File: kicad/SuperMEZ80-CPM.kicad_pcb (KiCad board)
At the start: 2 copper layers, 61 x 57.1 mm, 36 parts, among them J1 EMUZ80_0, J2 EMUZ80, J3 Conn_02x03_Odd_Even, J4 Conn_02x01, J5 Conn_02x02_Odd_Even, J6 SD Card slot, J7 SD Card slot, U1 Z80CPU, U2 AS6C4008

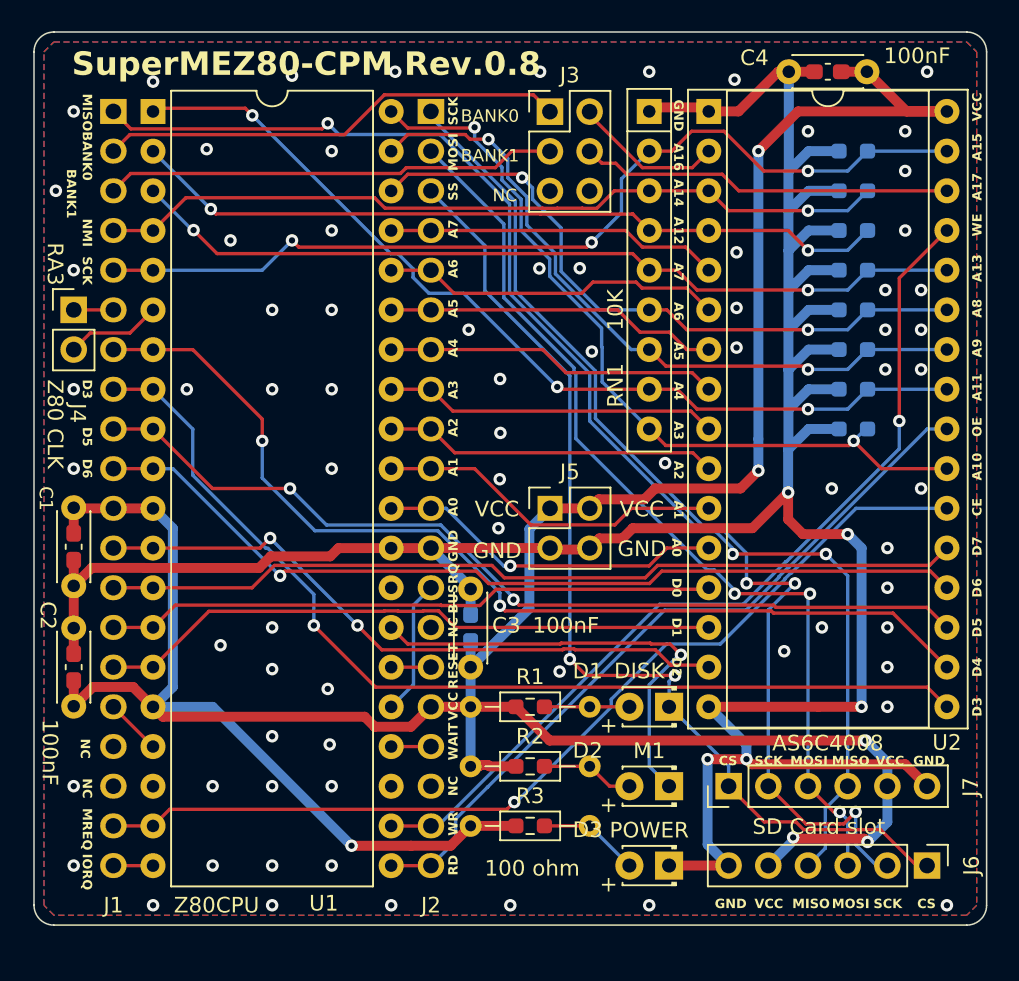
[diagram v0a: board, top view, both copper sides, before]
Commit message: Add SuperMEZ80-CPM version 1.0
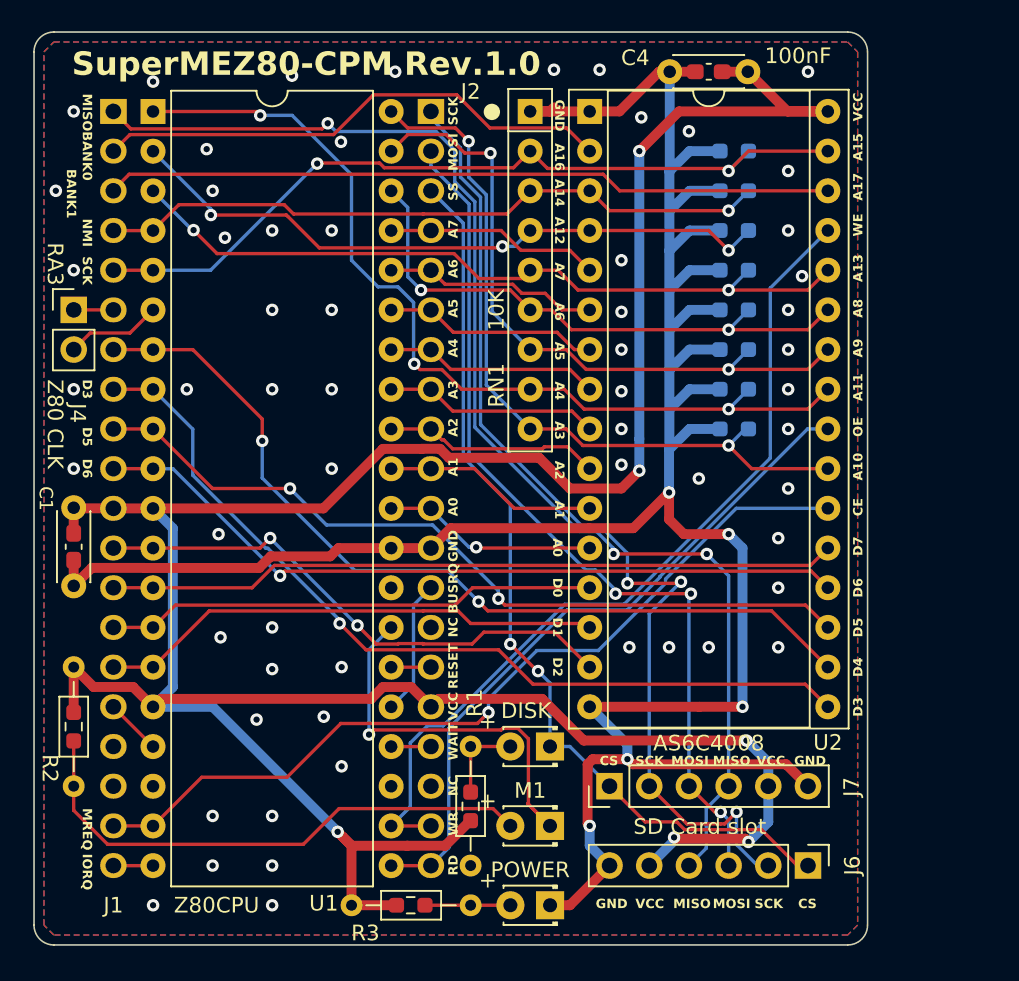
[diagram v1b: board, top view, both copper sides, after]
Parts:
- removed C2, C3: 100nF, Capacitor_THT:C_Disc_D4.3mm_W1.9mm_P5.00mm
- removed C6, C7: 100nF, Capacitor_SMD:C_0603_1608Metric_Pad1.08x0.95mm_HandSolder
- removed J3: Conn_02x03_Odd_Even, Connector_PinHeader_2.54mm:PinHeader_2x03_P2.54mm_Vertical
- removed J5: Conn_02x02_Odd_Even, Connector_PinHeader_2.54mm:PinHeader_2x02_P2.54mm_Vertical
- moved R5 29.3 mm to (78.7, 101.6), turned to -90 degrees
- moved R2 26.2 mm to (78.7, 97.8), turned to -90 degrees
- moved R1 10.2 mm to (104.1, 110.5), turned to 90 degrees
- moved R6 9.18 mm to (100.3, 113.0)
- moved R3 9.16 mm to (96.5, 113.0)
- moved D1 8.03 mm to (109.2, 102.9)
- moved D2 8.03 mm to (109.2, 108.0)
- moved D3 8.03 mm to (109.2, 113.0)
- moved C4 7.62 mm to (121.9, 59.7)
- moved C8 7.62 mm to (119.4, 59.7)
- moved J7 7.62 mm to (113.0, 105.4)
- moved R10 7.62 mm to (121.0, 72.4)
- moved R11 7.62 mm to (121.0, 74.9)
- moved R12 7.62 mm to (121.0, 77.5)
- moved R13 7.62 mm to (121.0, 80.0)
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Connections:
- J1 pad 2: BANK0 -> A16
- J1 pad 3: BANK1 -> A17
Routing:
- net BANK0: track 29.9 -> 0.00 mm
- net BANK1: track 29.0 -> 0.00 mm
- net Net-(D2-A): track 5.96 -> 34.7 mm
- net A16: track 9.67 -> 33.5 mm
- net A17: track 23.9 -> 46.6 mm
- net GND: track 185.9 -> 171.3 mm, vias 79 -> 65
- net D3: track 64.7 -> 56.0 mm
- net A0: track 22.3 -> 13.8 mm
- net A1: track 22.3 -> 13.8 mm
- net D7: track 55.1 -> 46.8 mm
- net D6: track 57.4 -> 49.1 mm
- net A15: track 60.2 -> 52.0 mm, vias 3 -> 2
- net A6: track 22.0 -> 13.8 mm
- net D4: track 64.5 -> 56.3 mm
- net D1: track 40.1 -> 32.1 mm
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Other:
- board size 61 x 57.1 mm -> 53.3 x 58.4 mm
- board text added: "Aug 17, 2023 @hanyazou"
- board text added: "SuperMEZ80-CPM Rev.1.0"
- board text added: "●"
- board text removed: "100 ohm"
- board text removed: "Jul 8, 2023 @hanyazou"
- board text removed: "SuperMEZ80-CPM Rev.0.8"

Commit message: Add SuperMEZ80-CPM version 1.1 and update README.md
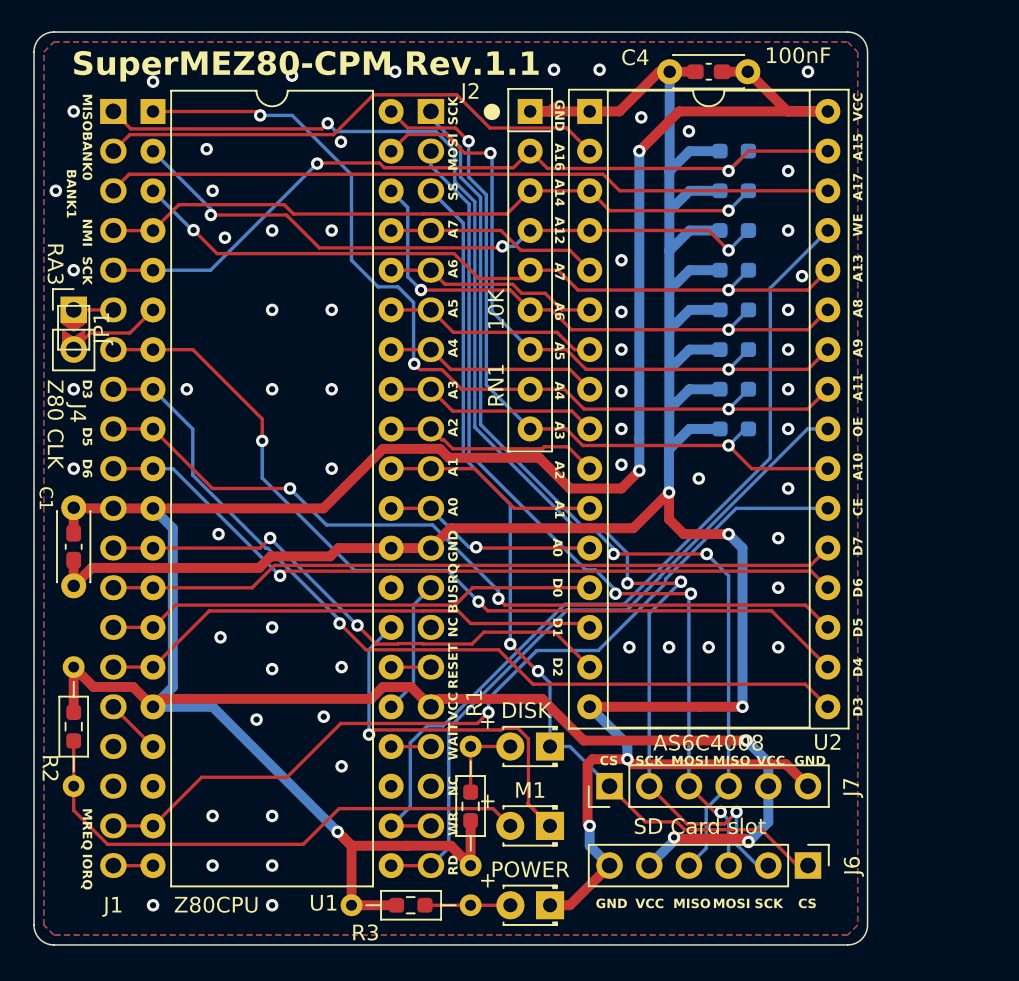
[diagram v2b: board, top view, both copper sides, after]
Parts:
- added JP1: Jumper_2_Open, Jumper:SolderJumper-2_P1.3mm_Open_TrianglePad1.0x1.5mm, F.Cu at (78.7, 76.1)
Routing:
- net VCC: track 192.6 -> 195.3 mm
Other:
- board text added: "Aug 25, 2023 @hanyazou"
- board text added: "SuperMEZ80-CPM Rev.1.1"
- board text removed: "Aug 17, 2023 @hanyazou"
- board text removed: "SuperMEZ80-CPM Rev.1.0"
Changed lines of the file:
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@@
       (drillshape 0)
       (scaleselection 1)
-      (outputdirectory "SuperMEZ80-CPM-1.0")
+      (outputdirectory "SuperMEZ80-CPM-1.1")
     )
   )
@@
     )
   )
+  (footprint "Jumper:SolderJumper-2_P1.3mm_Open_TrianglePad1.0x1.5mm" (layer "F.Cu")
+    (at 78.74 76.073 -90)
+    (descr "SMD Solder Jumper, 1x1.5mm Triangular Pads, 0.3mm gap, open")
+    (tags "solder jumper open")
+    (property "Sheetfile" "SuperMEZ80-CPM.kicad_sch")
+    (property "Sheetname" "")
+    (property "ki_description" "Jumper, 2-pole, open")
+    (property "ki_keywords" "Jumper SPST")
+    (attr exclude_from_pos_files)
+    (fp_text reference "JP1" (at 0 -1.8 90) (layer "F.SilkS")
+        (effects (font (size 1 1) (thickness 0.15)))
+    )
+    (fp_text value "Jumper_2_Open" (at 0 1.9 90) (layer "F.Fab")
+        (effects (font (size 1 1) (thickness 0.15)))
+    )
+    (fp_line (start -1.4 -1) (end 1.4 -1)
+      (stroke (width 0.12) (type solid)) (layer "F.SilkS"))
+    (fp_line (start -1.4 1) (end -1.4 -1)
+      (stroke (width 0.12) (type solid)) (layer "F.SilkS"))
+    (fp_line (start 1.4 -1) (end 1.4 1)
+      (stroke (width 0.12) (type solid)) (layer "F.SilkS"))
+    (fp_line (start 1.4 1) (end -1.4 1)
+      (stroke (width 0.12) (type solid)) (layer "F.SilkS"))
+    (fp_line (start -1.65 -1.25) (end -1.65 1.25)
+      (stroke (width 0.05) (type solid)) (layer "F.CrtYd"))
+    (fp_line (start -1.65 -1.25) (end 1.65 -1.25)
+      (stroke (width 0.05) (type solid)) (layer "F.CrtYd"))
+    (fp_line (start 1.65 1.25) (end -1.65 1.25)
+      (stroke (width 0.05) (type solid)) (layer "F.CrtYd"))
+    (fp_line (start 1.65 1.25) (end 1.65 -1.25)
+      (stroke (width 0.05) (type solid)) (layer "F.CrtYd"))
+    (pad "1" smd custom (at -0.725 0 270) (size 0.3 0.3) (layers "F.Cu" "F.Mask")
+      (net 6 "RA3") (pinfunction "A") (pintype "passive") (zone_connect 2) (thermal_bridge_angle 45)
+      (options (clearance outline) (anchor rect))
+      (primitives
+        (gr_poly
+          (pts
+            (xy 1 0)
+            (xy 0.5 0.75)
+            (xy -0.5 0.75)
+            (xy -0.5 -0.75)
+            (xy 0.5 -0.75)
+          )
+          (width 0) (fill yes))
+      ))
+    (pad "2" smd custom (at 0.725 0 270) (size 0.3 0.3) (layers "F.Cu" "F.Mask")
+      (net 40 "CLK") (pinfunction "B") (pintype "passive") (zone_connect 2) (thermal_bridge_angle 45)
+      (options (clearance outline) (anchor rect))
+      (primitives
+        (gr_poly
+          (pts
+            (xy 0.5 0.75)
+            (xy -0.65 0.75)
+            (xy -0.15 0)
+            (xy -0.65 -0.75)
+            (xy 0.5 -0.75)
+          )
+          (width 0) (fill yes))
+      ))
+  )
   (footprint "Package_DIP:DIP-40_W15.24mm" (layer "F.Cu")
     (at 83.815 62.235)
@@
     (effects (font (size 0.8 0.8) (thickness 0.15) bold) (justify left bottom mirror))
   )
-  (gr_text "Aug 17, 2023 @hanyazou" (at 88.519 104.902 270) (layer "B.SilkS")
+  (gr_text "Aug 25, 2023 @hanyazou" (at 88.519 104.902 270) (layer "B.SilkS")
     (effects (font (size 1.5 1.5) (thickness 0.3) bold) (justify left bottom mirror))
   )
-  (gr_text "SuperMEZ80-CPM Rev.1.0" (at 92.71 104.902 270) (layer "B.SilkS")
+  (gr_text "SuperMEZ80-CPM Rev.1.1" (at 92.71 104.902 270) (layer "B.SilkS")
     (effects (font (size 1.5 1.5) (thickness 0.3) bold) (justify left bottom mirror))
   )
@@
     (effects (font (size 0.6 0.6) (thickness 0.12) bold) (justify left bottom))
   )
-  (gr_text "SuperMEZ80-CPM Rev.1.0" (at 78.613 60.071) (layer "F.SilkS")
+  (gr_text "SuperMEZ80-CPM Rev.1.1" (at 78.613 60.071) (layer "F.SilkS")
     (effects (font (size 1.5 1.5) (thickness 0.3) bold) (justify left bottom))
   )
@@
   (segment (start 81.285 87.635) (end 81.28 87.63) (width 0.635) (layer "F.Cu") (net 1))
   (segment (start 117.475 62.23) (end 114.935 64.77) (width 0.635) (layer "F.Cu") (net 1))
-  (segment (start 104.14 107.5925) (end 102.5126 109.2199) (width 0.635) (layer "F.Cu") (net 1))
   (segment (start 121.92 108.977651) (end 121.711998 108.769649) (width 0.635) (layer "F.Cu") (net 1))
   (segment (start 83.815 100.335) (end 82.5401 99.0601) (width 0.635) (layer "F.Cu") (net 1))
   (segment (start 96.52 109.22) (end 95.9485 108.6485) (width 0.635) (layer "F.Cu") (net 1))
   (segment (start 121.793 102.489) (end 111.379 102.489) (width 0.635) (layer "F.Cu") (net 1))
+  (segment (start 100.0759 109.2199) (end 102.8699 109.2199) (width 0.635) (layer "F.Cu") (net 1))
   (segment (start 95.9485 108.6485) (end 95.631 108.331) (width 0.635) (layer "F.Cu") (net 1))
-  (segment (start 96.5249 109.2249) (end 95.9485 108.6485) (width 0.635) (layer "F.Cu") (net 1))
   (segment (start 102.108 99.822) (end 101.6 100.33) (width 0.635) (layer "F.Cu") (net 1))
   (segment (start 96.52 113.03) (end 96.52 109.22) (width 0.635) (layer "F.Cu") (net 1))
@@
   (segment (start 101.02399 83.8201) (end 102.17601 83.8201) (width 0.635) (layer "F.Cu") (net 1))
   (segment (start 108.527351 84.397351) (end 110.4899 86.3599) (width 0.635) (layer "F.Cu") (net 1))
-  (segment (start 102.5126 109.2199) (end 100.0759 109.2199) (width 0.635) (layer "F.Cu") (net 1))
+  (segment (start 100.0709 109.2249) (end 100.0759 109.2199) (width 0.635) (layer "F.Cu") (net 1))
+  (segment (start 104.14 107.616) (end 104.14 110.49) (width 0.635) (layer "F.Cu") (net 1))
   (segment (start 78.74 100.6875) (end 78.74 97.79) (width 0.635) (layer "F.Cu") (net 1))
+  (segment (start 95.9485 108.6485) (end 96.5249 109.2249) (width 0.635) (layer "F.Cu") (net 1))
   (segment (start 97.77209 99.822) (end 98.52899 99.0651) (width 0.635) (layer "F.Cu") (net 1))
   (segment (start 78.78 87.63) (end 78.74 87.59) (width 0.635) (layer "F.Cu") (net 1))
-  (segment (start 100.0759 109.2199) (end 100.0709 109.2249) (width 0.635) (layer "F.Cu") (net 1))
   (segment (start 84.328 99.822) (end 97.77209 99.822) (width 0.635) (layer "F.Cu") (net 1))
   (segment (start 98.52899 83.8251) (end 101.01899 83.8251) (width 0.635) (layer "F.Cu") (net 1))
@@
   (segment (start 102.753261 84.397351) (end 108.527351 84.397351) (width 0.635) (layer "F.Cu") (net 1))
   (segment (start 100.3351 99.0651) (end 101.6 100.33) (width 0.635) (layer "F.Cu") (net 1))
+  (segment (start 96.5249 109.2249) (end 100.0709 109.2249) (width 0.635) (layer "F.Cu") (net 1))
+  (segment (start 102.8699 109.2199) (end 104.14 110.49) (width 0.635) (layer "F.Cu") (net 1))
   (segment (start 108.712 99.822) (end 102.108 99.822) (width 0.635) (layer "F.Cu") (net 1))
   (segment (start 83.815 100.335) (end 84.328 99.822) (width 0.635) (layer "F.Cu") (net 1))
@@
   (segment (start 113.7921 86.3599) (end 114.935 85.217) (width 0.635) (layer "F.Cu") (net 1))
   (segment (start 102.17601 83.8201) (end 102.753261 84.397351) (width 0.635) (layer "F.Cu") (net 1))
-  (segment (start 100.0709 109.2249) (end 96.5249 109.2249) (width 0.635) (layer "F.Cu") (net 1))
   (via (at 121.92 108.977651) (size 0.8) (drill 0.4) (layers "F.Cu" "B.Cu") (net 1))
   (via (at 95.631 108.331) (size 0.8) (drill 0.4) (layers "F.Cu" "B.Cu") (net 1))

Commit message: Add SuperMEZ80-CPM version 1.2
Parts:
- added R15: 10K, Resistor_SMD:R_0603_1608Metric_Pad0.98x0.95mm_HandSolder, B.Cu at (95.9, 94.0)
- JP1: footprint Jumper:SolderJumper-2_P1.3mm_Open_TrianglePad1.0x1.5mm -> Jumper:SolderJumper-2_P1.3mm_Open_RoundedPad1.0x1.5mm; moved to B.Cu
- moved JP1 13.3 mm to (91.5, 72.5)
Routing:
- net RA3: track 2.54 -> 14.1 mm
- net CLK: track 6.13 -> 15.2 mm
- net ~{RESET}: track 2.55 -> 7.89 mm, vias 0 -> 1
- net D5: track 51.3 -> 56.3 mm
- net GND: track 171.3 -> 174.2 mm, vias 65 -> 64
- net D4: track 56.3 -> 54.2 mm
- net D3: track 56.0 -> 57.1 mm
- net D2: track 34.8 -> 34.3 mm
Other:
- board text added: "Sep 19, 2023 @hanyazou"
- board text added: "SuperMEZ80-CPM Rev.1.2"
- board text removed: "Aug 25, 2023 @hanyazou"
- board text removed: "SuperMEZ80-CPM Rev.1.1"
